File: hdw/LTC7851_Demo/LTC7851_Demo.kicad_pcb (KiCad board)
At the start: 4 copper layers, 100 x 50 mm, 201 parts, among them J1101 FG_LOAD, J1102 ISNS, J1401 VOUT, J1402 LOOP_TAP, J1403 Wave_Gen_In, J201 +12V IN, J206 GND IN, J301 CLKOUT, J302 RUN, J303 SMOD, J304 IAVG, J901 +5V OUT, J902 +5V OUT, J903 GND OUT, J904 GND OUT, Q1101 BSC123N10LSGATMA1, Q1102 BSC123N10LSGATMA1, Q1201 BSC123N10LSGATMA1, Q1202 BSC123N10LSGATMA1, Q1301 BSC123N10LSGATMA1, Q1302 BSC123N10LSGATMA1, Q201 BSC123N10LSGATMA1, Q202 BSC123N10LSGATMA1, T1401 1:1 Pulse Transformer, U1101 LT1010DD, U201 LTC4365DDB, U202 74LVC1G06, U301 LTC7851UHH, U302 74LVC1G17, U303 74LVC1G06, U304 74LVC1G06, U401 SiC779, U501 SiC779, U601 SiC779, U701 SiC779, U801 LM1117-ADJ

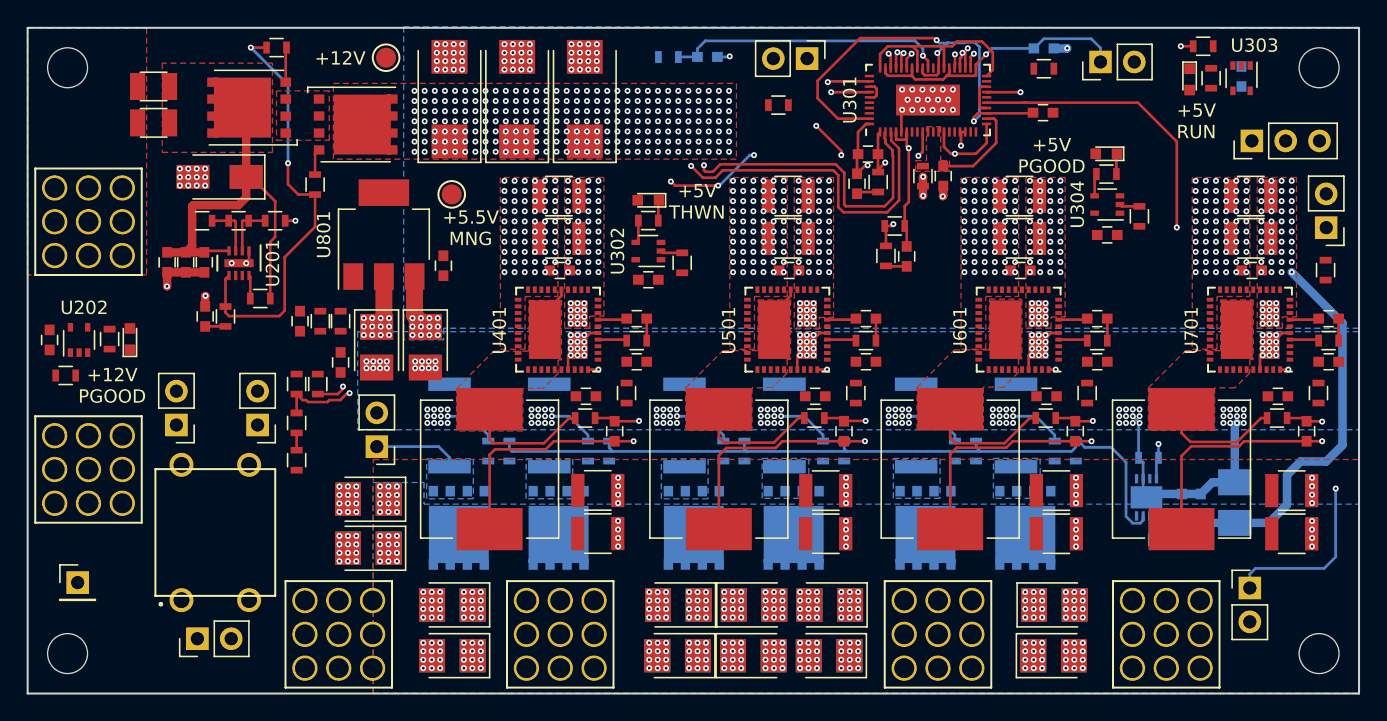
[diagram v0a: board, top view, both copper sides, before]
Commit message: More routing, silkscreen labels
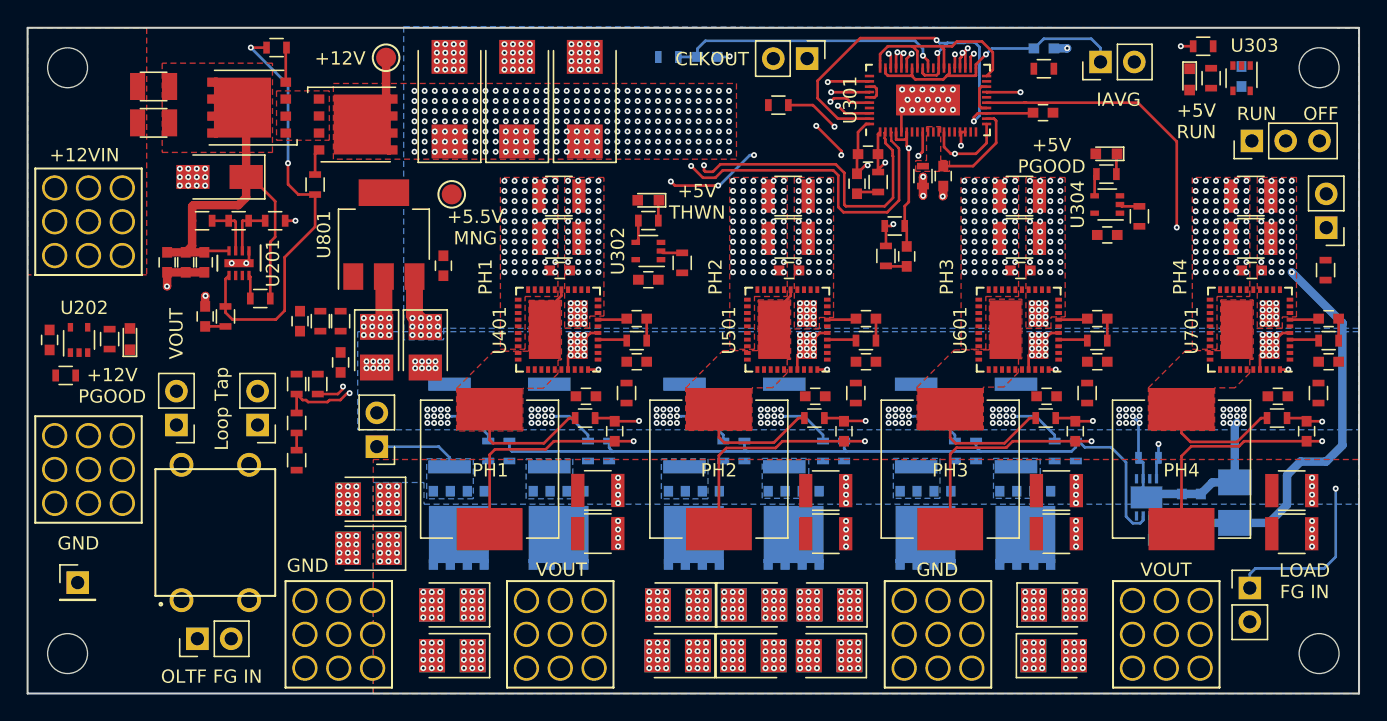
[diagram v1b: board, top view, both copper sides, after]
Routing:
- net Net-(J301-Pad1): track 0.00 -> 8.73 mm, vias 0 -> 1
- net Net-(R303-Pad1): track 0.00 -> 8.42 mm, vias 0 -> 2
- net +12V: track 38.9 -> 44.6 mm
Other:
- board text added: "+12VIN"
- board text added: "CLKOUT"
- board text added: "GND"
- board text added: "IAVG"
- board text added: "LOAD FG IN"
- board text added: "Loop Tap"
- board text added: "OFF"
- board text added: "OLTF FG IN"
- board text added: "PH1"
- board text added: "PH2"
- board text added: "PH3"
- board text added: "PH4"
- board text added: "RUN"
- board text added: "SMOD"
- board text added: "VOUT"
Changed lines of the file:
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@@
   (general
     (thickness 1.6)
-    (drawings 10)
-    (tracks 1983)
+    (drawings 33)
+    (tracks 2004)
     (zones 0)
     (modules 201)
@@
       (net 2 GND))
   )
+  (gr_text SMOD (at 173.0248 81.3308 90) (layer B.SilkS)
+    (effects (font (size 1 1) (thickness 0.15)) (justify mirror))
+  )
+  (gr_text OFF (at 174.498 73.7616) (layer F.SilkS)
+    (effects (font (size 1 1) (thickness 0.15)))
+  )
+  (gr_text RUN (at 169.672 73.7616) (layer F.SilkS)
+    (effects (font (size 1 1) (thickness 0.15)))
+  )
+  (gr_text PH4 (at 163.9316 86.0044 90) (layer F.SilkS)
+    (effects (font (size 1 1) (thickness 0.15)))
+  )
+  (gr_text PH3 (at 146.4056 86.0044 90) (layer F.SilkS)
+    (effects (font (size 1 1) (thickness 0.15)))
+  )
+  (gr_text PH2 (at 129.032 86.0044 90) (layer F.SilkS)
+    (effects (font (size 1 1) (thickness 0.15)))
+  )
+  (gr_text PH1 (at 111.76 86.0044 90) (layer F.SilkS)
+    (effects (font (size 1 1) (thickness 0.15)))
+  )
+  (gr_text PH4 (at 164.0332 100.5332) (layer F.SilkS)
+    (effects (font (size 1 1) (thickness 0.15)))
+  )
+  (gr_text PH3 (at 146.6596 100.5332) (layer F.SilkS)
+    (effects (font (size 1 1) (thickness 0.15)))
+  )
+  (gr_text PH2 (at 129.286 100.5332) (layer F.SilkS)
+    (effects (font (size 1 1) (thickness 0.15)))
+  )
+  (gr_text PH1 (at 112.1156 100.5332) (layer F.SilkS)
+    (effects (font (size 1 1) (thickness 0.15)))
+  )
+  (gr_text CLKOUT (at 128.778 69.6468) (layer F.SilkS)
+    (effects (font (size 1 1) (thickness 0.15)))
+  )
+  (gr_text VOUT (at 162.8648 108.0008) (layer F.SilkS)
+    (effects (font (size 1 1) (thickness 0.15)))
+  )
+  (gr_text GND (at 145.6944 108.0008) (layer F.SilkS)
+    (effects (font (size 1 1) (thickness 0.15)))
+  )
+  (gr_text VOUT (at 117.4496 108.0008) (layer F.SilkS)
+    (effects (font (size 1 1) (thickness 0.15)))
+  )
+  (gr_text GND (at 98.3996 107.696) (layer F.SilkS)
+    (effects (font (size 1 1) (thickness 0.15)))
+  )
+  (gr_text +12VIN (at 81.6356 76.8604) (layer F.SilkS)
+    (effects (font (size 1 1) (thickness 0.15)))
+  )
+  (gr_text GND (at 81.1784 106.0196) (layer F.SilkS)
+    (effects (font (size 1 1) (thickness 0.15)))
+  )
+  (gr_text "OLTF FG IN" (at 91.186 116.0272) (layer F.SilkS)
+    (effects (font (size 1 1) (thickness 0.15)))
+  )
+  (gr_text "Loop Tap" (at 91.948 95.9104 90) (layer F.SilkS)
+    (effects (font (size 1 1) (thickness 0.15)))
+  )
+  (gr_text VOUT (at 88.5444 90.2716 90) (layer F.SilkS)
+    (effects (font (size 1 1) (thickness 0.15)))
+  )
+  (gr_text "LOAD\nFG IN" (at 173.2788 108.8644) (layer F.SilkS)
+    (effects (font (size 1 1) (thickness 0.15)))
+  )
+  (gr_text IAVG (at 159.3088 72.6948) (layer F.SilkS)
+    (effects (font (size 1 1) (thickness 0.15)))
+  )
   (gr_text +12V (at 100.838 69.596) (layer F.SilkS)
     (effects (font (size 1 1) (thickness 0.15)))
   )
-  (gr_text "+5.5V\nMNG" (at 110.6424 82.3468) (layer F.SilkS)
+  (gr_text "+5.5V\nMNG" (at 110.998 82.296) (layer F.SilkS)
     (effects (font (size 1 1) (thickness 0.15)))
   )
@@
   (segment (start 170.5981 104.4839) (end 171.958 103.124) (width 0.635) (layer B.Cu) (net 3))
   (segment (start 174.9044 99.8728) (end 176.1236 98.6536) (width 0.635) (layer B.Cu) (net 3))
+  (segment (start 104.2924 72.7757) (end 102.5064 74.5617) (width 0.635) (layer F.Cu) (net 3))
+  (segment (start 104.2924 69.5452) (end 104.2924 72.7757) (width 0.635) (layer F.Cu) (net 3))
   (via (at 144.6276 79.9084) (size 0.45) (drill 0.2) (layers F.Cu B.Cu) (net 5))
   (segment (start 144.6149 79.1852) (end 144.6149 79.8957) (width 0.635) (layer F.Cu) (net 5))
@@
   (segment (start 159.1444 76.8088) (end 159.1944 76.7588) (width 0.2032) (layer F.Cu) (net 36))
   (segment (start 159.1444 78.2828) (end 159.1444 76.8088) (width 0.2032) (layer F.Cu) (net 36))
+  (segment (start 140.5959 72.9202) (end 139.2142 72.9202) (width 0.2032) (layer F.Cu) (net 38))
+  (segment (start 139.2142 72.9202) (end 138.8872 72.5932) (width 0.2032) (layer F.Cu) (net 38))
+  (via (at 137.668 72.8472) (size 0.45) (drill 0.2) (layers F.Cu B.Cu) (net 38))
+  (segment (start 138.8872 72.5932) (end 137.922 72.5932) (width 0.2032) (layer F.Cu) (net 38))
+  (segment (start 137.922 72.5932) (end 137.668 72.8472) (width 0.2032) (layer F.Cu) (net 38))
+  (segment (start 137.778701 72.736499) (end 137.981901 72.736499) (width 0.2032) (layer PWR) (net 38))
+  (segment (start 137.668 72.8472) (end 137.778701 72.736499) (width 0.2032) (layer PWR) (net 38))
+  (segment (start 137.981901 72.736499) (end 138.2776 72.4408) (width 0.2032) (layer PWR) (net 38))
+  (segment (start 138.2776 72.4408) (end 138.2776 70.3072) (width 0.2032) (layer PWR) (net 38))
+  (segment (start 137.5791 69.6087) (end 135.9154 69.6087) (width 0.2032) (layer PWR) (net 38))
+  (segment (start 138.2776 70.3072) (end 137.5791 69.6087) (width 0.2032) (layer PWR) (net 38))
   (segment (start 148.855399 71.867799) (end 149.002998 71.7202) (width 0.2032) (layer F.Cu) (net 39))
   (segment (start 149.002998 73.3202) (end 148.8948 73.212002) (width 0.2032) (layer F.Cu) (net 39))
@@
   (segment (start 94.1324 68.7832) (end 95.3128 68.7832) (width 0.2032) (layer F.Cu) (net 61))
   (segment (start 98.9584 82.2452) (end 98.9584 79.8202) (width 0.2032) (layer F.Cu) (net 61))
-  (segment (start 92.2274 88.6794) (end 92.4988 88.9508) (width 0.2032) (layer F.Cu) (net 61))
+  (segment (start 92.2274 88.6794) (end 92.7528 89.2048) (width 0.2032) (layer F.Cu) (net 61))
   (segment (start 92.2274 88.2262) (end 92.2274 88.6794) (width 0.2032) (layer F.Cu) (net 61))
-  (segment (start 92.4988 88.9508) (end 96.266 88.9508) (width 0.2032) (layer F.Cu) (net 61))
-  (segment (start 96.266 88.9508) (end 96.6724 88.5444) (width 0.2032) (layer F.Cu) (net 61))
+  (segment (start 92.7528 89.2048) (end 96.012 89.2048) (width 0.2032) (layer F.Cu) (net 61))
+  (segment (start 96.012 89.2048) (end 96.6724 88.5444) (width 0.2032) (layer F.Cu) (net 61))
   (segment (start 96.6724 88.5444) (end 96.6724 84.5312) (width 0.2032) (layer F.Cu) (net 61))
   (segment (start 96.6724 84.5312) (end 98.9584 82.2452) (width 0.2032) (layer F.Cu) (net 61))
+  (segment (start 134.5064 73.1012) (end 136.3472 73.1012) (width 0.2032) (layer F.Cu) (net 64))
+  (via (at 137.9728 74.7268) (size 0.45) (drill 0.2) (layers F.Cu B.Cu) (net 64))
+  (segment (start 136.3472 73.1012) (end 137.9728 74.7268) (width 0.2032) (layer F.Cu) (net 64))
+  (segment (start 137.9728 74.7268) (end 138.2268 74.4728) (width 0.2032) (layer PWR) (net 64))
+  (via (at 138.2268 73.152) (size 0.45) (drill 0.2) (layers F.Cu B.Cu) (net 64))
+  (segment (start 138.2268 74.4728) (end 138.2268 73.152) (width 0.2032) (layer PWR) (net 64))
+  (segment (start 138.795 73.7202) (end 138.2268 73.152) (width 0.2032) (layer F.Cu) (net 64))
+  (segment (start 140.5959 73.7202) (end 138.795 73.7202) (width 0.2032) (layer F.Cu) (net 64))
   (segment (start 125.0791 84.2003) (end 124.9401 84.0613) (width 0.2032) (layer F.Cu) (net 65))
   (segment (start 126.5301 84.2003) (end 125.0791 84.2003) (width 0.2032) (layer F.Cu) (net 65))

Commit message: Finished ROUTING (for the most part)
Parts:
- removed J303: SMOD, Pin_Headers:Pin_Header_Straight_1x02_Pitch2.54mm
- removed R309: 10k, Resistors_SMD:R_0603
- moved R401 1.98 mm to (151.7, 70.3)
- moved J301 0.08 mm to (135.8, 69.6)
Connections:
- U401 pad 1: POS5_SMOD -> (no net)
- U401 pad 39: POS5_RUN -> +5.5V_MNG
- U501 pad 1: POS5_SMOD -> (no net)
- U501 pad 39: POS5_RUN -> +5.5V_MNG
- U601 pad 1: POS5_SMOD -> (no net)
- U601 pad 39: POS5_RUN -> +5.5V_MNG
- U701 pad 1: POS5_SMOD -> (no net)
- U701 pad 39: POS5_RUN -> +5.5V_MNG
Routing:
- net ~POS5_THDN: track 1.65 -> 76.6 mm, vias 0 -> 10
- net POS5_RUN: track 4.22 -> 61.5 mm, vias 0 -> 2
- net +5.5V_MNG: track 5.42 -> 59.1 mm, vias 14 -> 33
- net POS5_PGOOD_OC: track 1.52 -> 46.7 mm, vias 0 -> 8
- net GND: track 73.2 -> 113.8 mm, vias 662 -> 675
- net +12V: track 44.6 -> 70.6 mm, vias 444 -> 445
- net +5V: track 241.0 -> 263.8 mm
- net POS12_PGOOD: track 0.00 -> 20.7 mm, vias 0 -> 2
- net Net-(C411-Pad1): track 0.00 -> 7.78 mm
- net Net-(C606-Pad1): track 0.00 -> 7.63 mm
- net Net-(C706-Pad1): track 0.00 -> 7.45 mm
- net LOOP_TAP: track 1.29 -> 8.58 mm
- net Net-(C506-Pad1): track 0.00 -> 7.09 mm
- net Net-(C803-Pad1): track 0.00 -> 6.04 mm
- net Net-(Q1301-Pad4): track 0.00 -> 3.98 mm
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- added copper zone on F.Cu, net +5.5V_MNG
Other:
- board text added: "LD ISNS"
- board text removed: "SMOD"

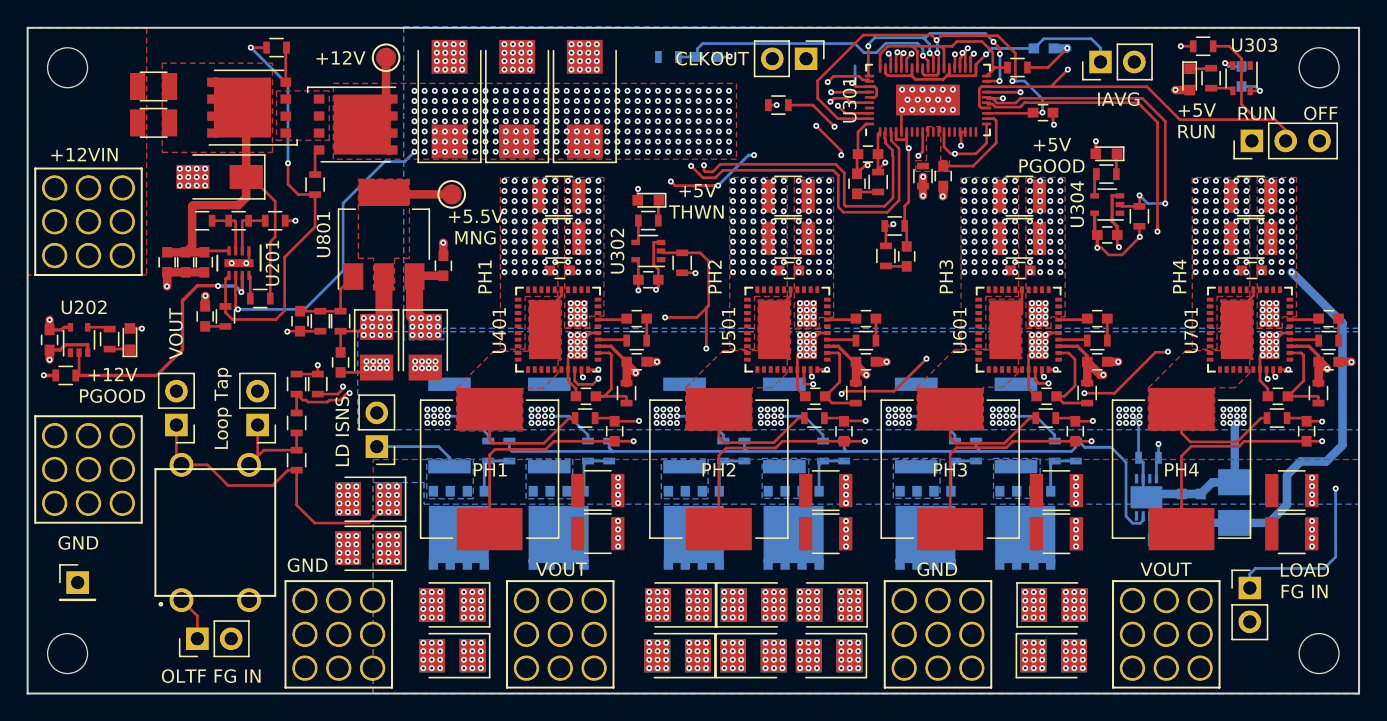
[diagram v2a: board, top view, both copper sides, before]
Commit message: Finished routing, added 3D render png, ordered PCB
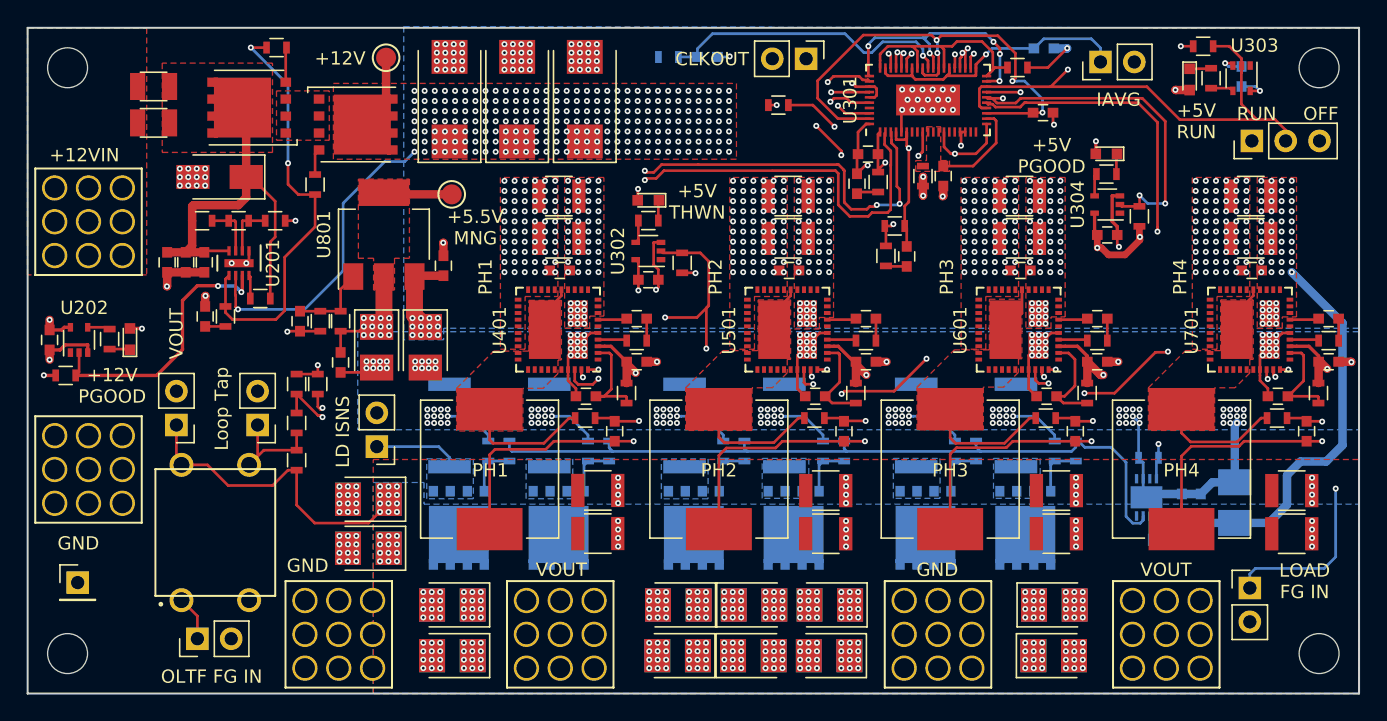
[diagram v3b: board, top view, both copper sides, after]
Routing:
- net /POS5 Phase 1/POS5_VSNS1_-: track 67.1 -> 69.3 mm, vias 2 -> 4
- net /POS5 Phase 1/POS5_VSNS1_+: track 70.0 -> 71.7 mm
- net POS5_RUN: track 61.5 -> 60.1 mm
- net Net-(C302-Pad1): track 21.5 -> 22.2 mm
- net Net-(U301-Pad52): track 36.6 -> 36.2 mm, vias 5 -> 2
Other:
- board text added: "LTC7851 Demo Board Four Phase 1MHz 5V 80A Buck"

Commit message: Added a few connectors and cleaned up some routing
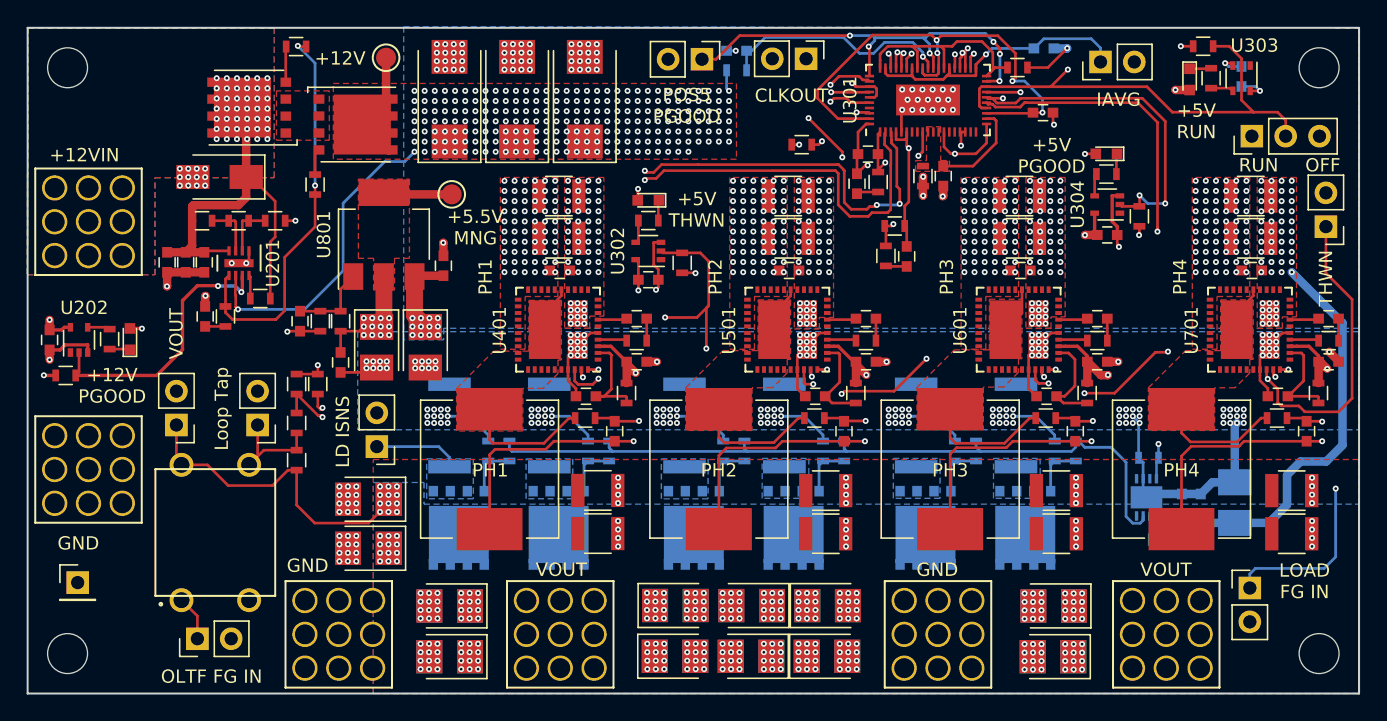
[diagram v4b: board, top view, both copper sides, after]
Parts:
- removed F201, F202: 25A, Fuse_Holders_and_Fuses:Fuse_SMD1206_Reflow
- added J303: THDN, Pin_Headers:Pin_Header_Straight_1x02_Pitch2.54mm, F.Cu at (174.9, 82.2)
- added J305: PGOOD, Pin_Headers:Pin_Header_Straight_1x02_Pitch2.54mm, F.Cu at (128.0, 69.7)
- Q1101, Q1102, Q1201, Q1202, Q1301, Q1302, Q201, Q202: value BSC123N10LSGATMA1 -> IPC100N04S51R7ATMA1
- moved R302 5.22 mm to (130.6, 70.5)
- moved C601 3.89 mm to (154.4, 114.5), turned to 180 degrees
- moved C615 3.89 mm to (154.4, 114.5), turned to 180 degrees
- moved C507 3.87 mm to (137.4, 114.5), turned to 0 degrees
- moved C702 3.87 mm to (137.4, 114.5), turned to 0 degrees
- moved C503 3.87 mm to (131.7, 114.5), turned to 180 degrees
- moved C505 3.87 mm to (131.7, 114.5), turned to 180 degrees
- moved C407 3.86 mm to (126.0, 114.5), turned to 0 degrees
- moved C607 3.86 mm to (126.0, 114.5), turned to 0 degrees
- moved C405 3.77 mm to (126.0, 110.7), turned to 0 degrees
- moved C412 3.77 mm to (126.0, 110.7), turned to 0 degrees
- moved C502 3.76 mm to (131.7, 110.7), turned to 180 degrees
- moved C605 3.76 mm to (131.7, 110.7), turned to 180 degrees
- moved C603 3.76 mm to (137.5, 110.7), turned to 0 degrees
- moved C701 3.76 mm to (137.5, 110.7), turned to 0 degrees
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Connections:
- J201 pad 1: Net-(F201-Pad2) -> +12Vin
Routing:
- net ~POS5_THDN: track 76.6 -> 98.6 mm
- net POS5_PGOOD_OC: track 46.7 -> 60.5 mm, vias 8 -> 9
- net Net-(C302-Pad1): track 22.2 -> 17.6 mm
- net +5.5V_MNG: track 59.2 -> 55.2 mm
- net Net-(R303-Pad1): track 8.42 -> 5.37 mm
- net Net-(R205-Pad1): track 32.4 -> 29.8 mm
- net +5V: track 263.8 -> 265.7 mm
- net +12V: track 70.6 -> 72.2 mm, vias 445 -> 441
- net Net-(U301-Pad52): track 36.2 -> 35.2 mm
- net /POS5 Phase 2/POS5_ISNS2_+: track 43.3 -> 43.9 mm
- net POS5_RUN: track 60.1 -> 59.5 mm
- net /POS5 Phase 3/POS5_ISNS3_+: track 38.7 -> 39.3 mm
- net +12Vin: vias 0 -> 42
- added copper zone on B.Cu, net +12Vin
- removed copper zone on F.Cu, net Net-(F201-Pad2)
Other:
- board text added: "POS5 PGOOD"
- board text added: "THWN"
